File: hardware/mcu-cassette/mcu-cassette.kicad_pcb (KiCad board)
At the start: 2 copper layers, 80.4 x 50 mm, 4 parts, among them J1 02x15_Horinzontal_Header

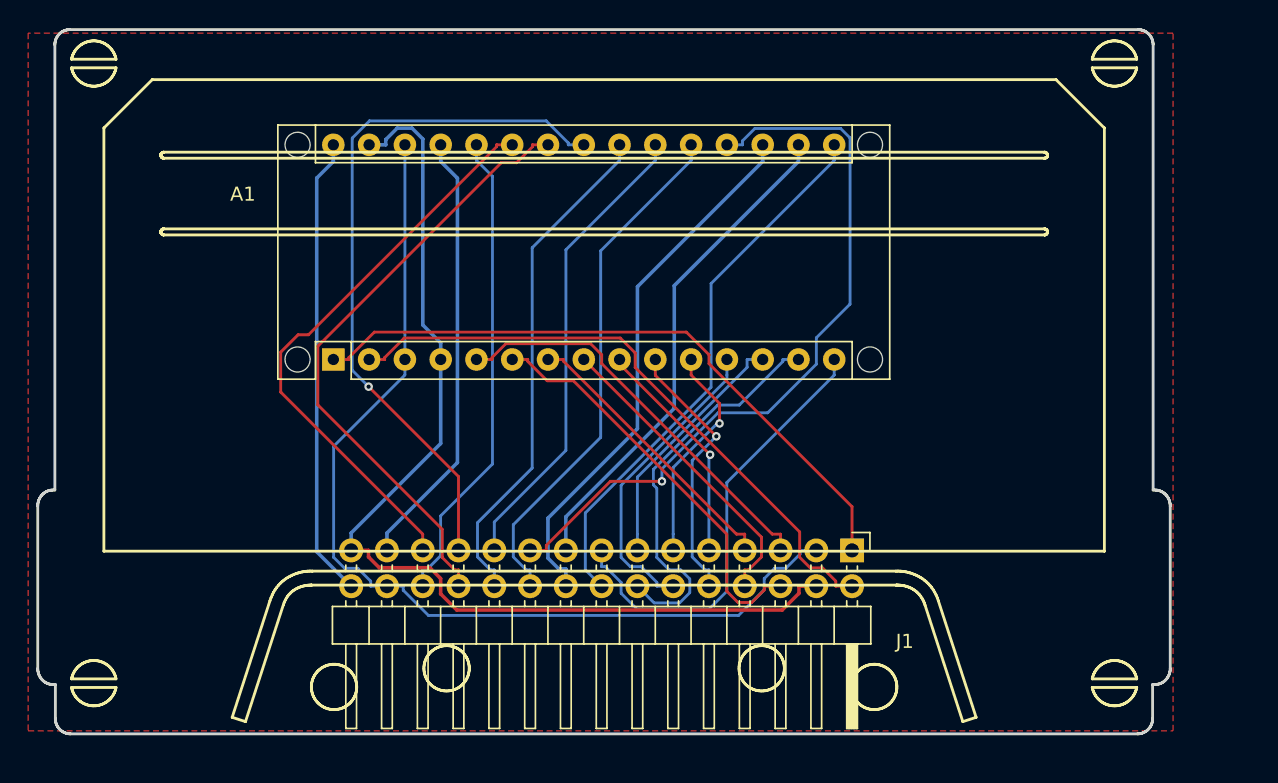
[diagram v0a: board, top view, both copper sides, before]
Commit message: [hw] Move copper pour to back layer, Add signature, Update pcb images
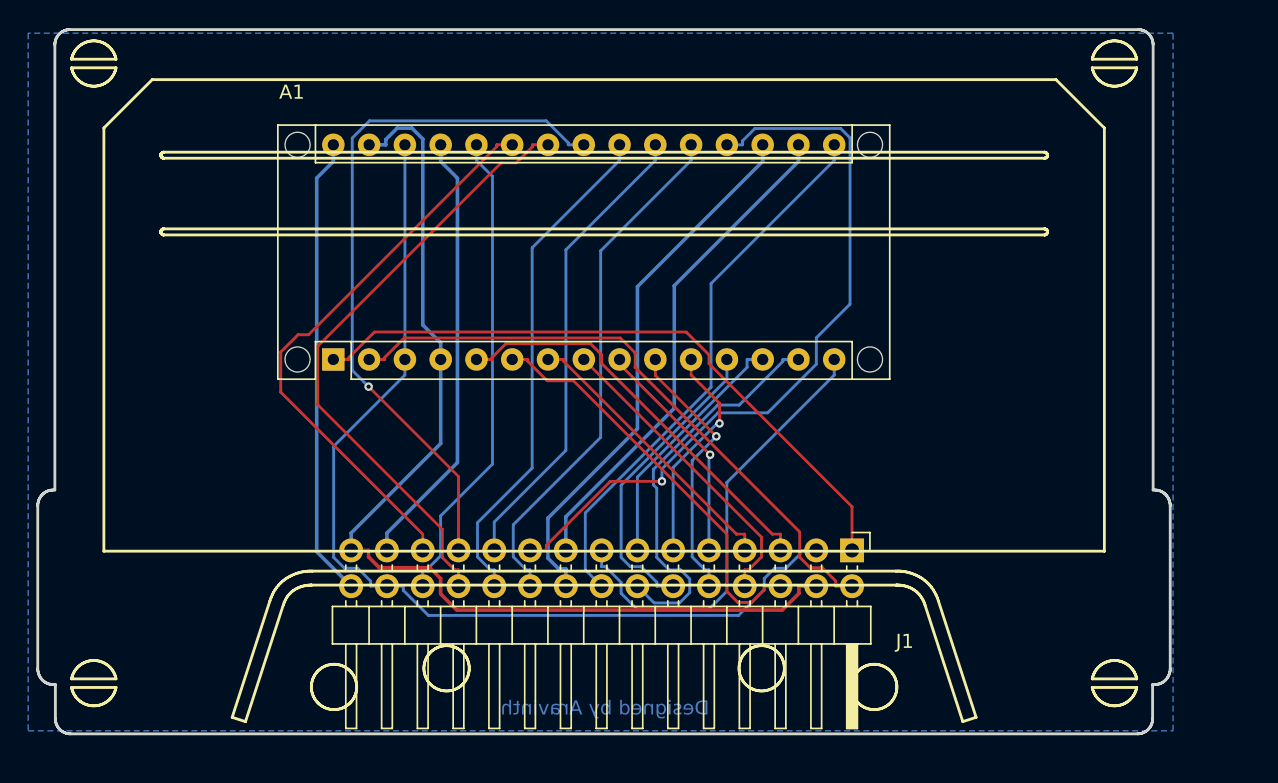
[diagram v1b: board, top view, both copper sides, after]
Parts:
- added REF**: CASSETTE-MARK, ARABEAT:CASSETTE-MARK, F.Cu at (94.5, 98.6)
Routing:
- added copper zone on B.Cu, net GND
- removed copper zone on F.Cu, net GND
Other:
- board text added: "Designed by Aravinth"

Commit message: [hw] Update libraries of MCU Cassette
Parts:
- G***: footprint ARABEAT:LOGO -> MCU-CASSETTE:LOGO
- REF**: footprint ARABEAT:CASSETTE-MARK -> MCU-CASSETTE:CASSETTE-MARK
- REF**: footprint ARABEAT:CASSETTE-SILKSCREEN -> MCU-CASSETTE:CASSETTE-SILKSCREEN

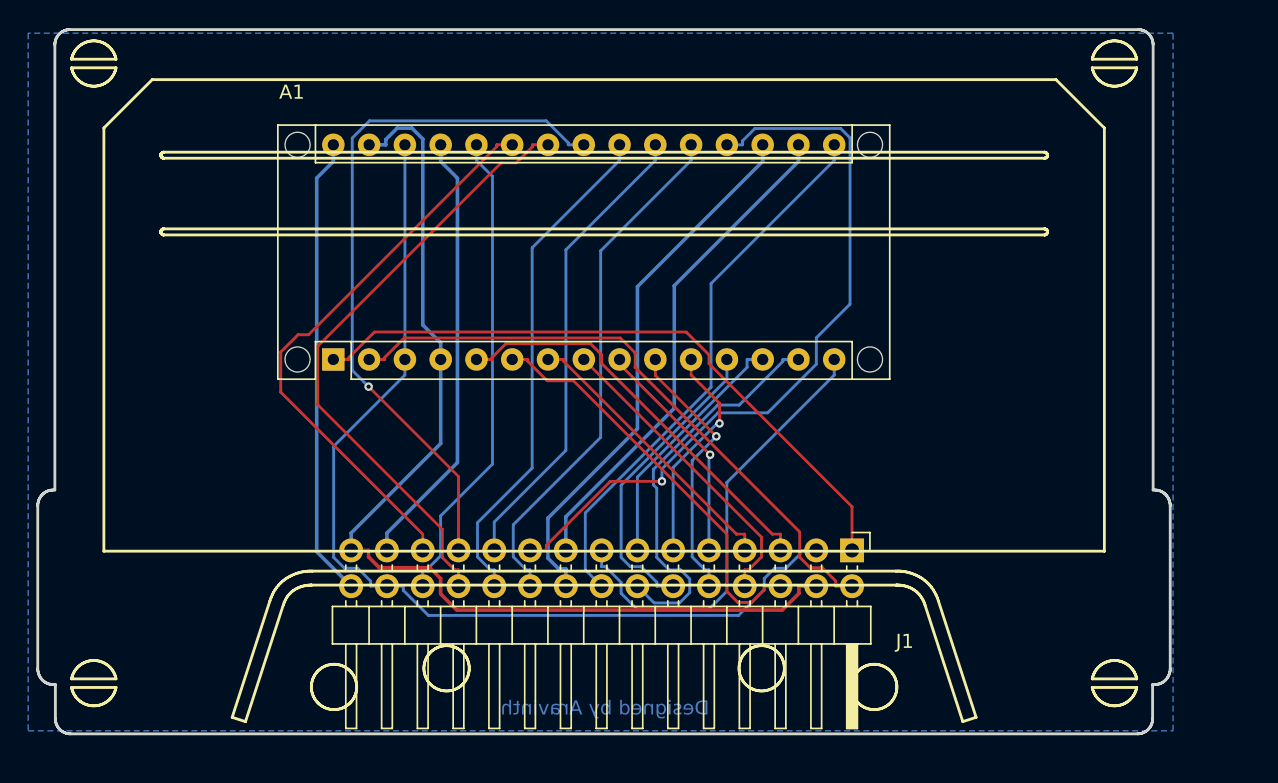
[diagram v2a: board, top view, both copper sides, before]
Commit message: [hw] Update MCU Cassette with new footprints
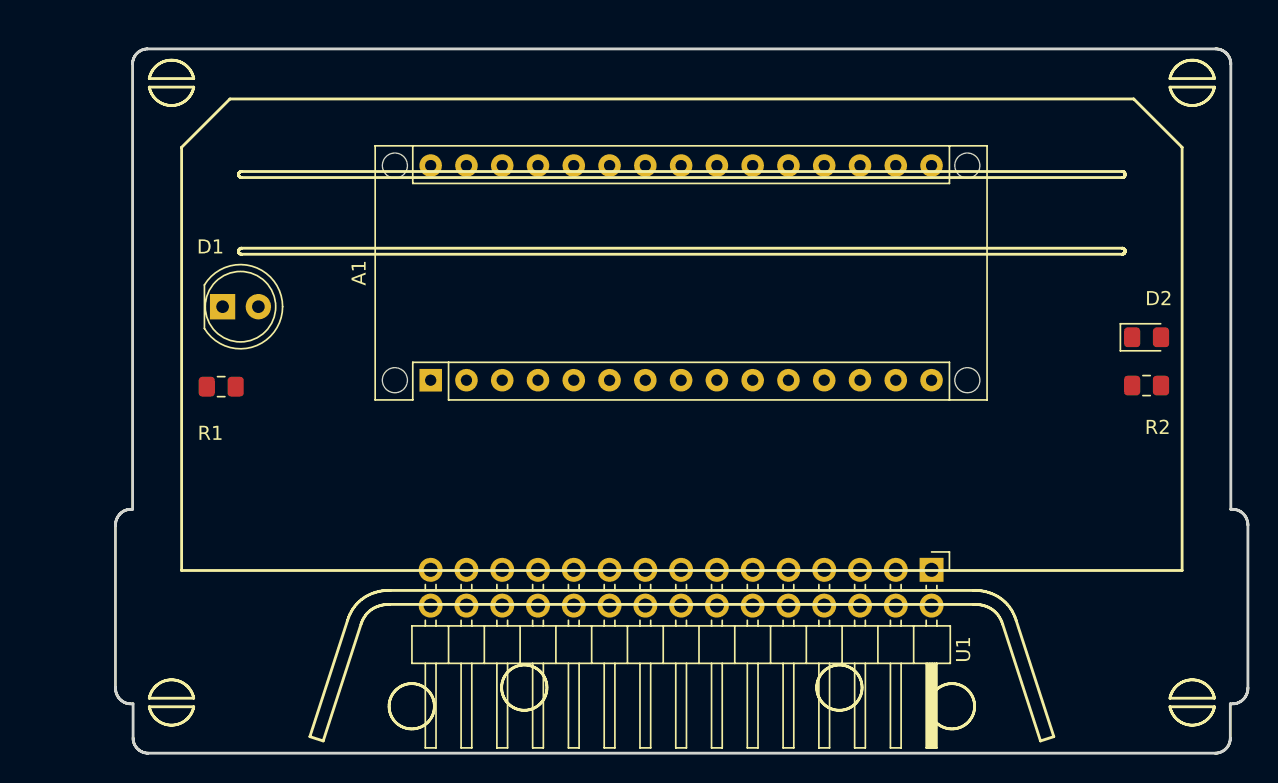
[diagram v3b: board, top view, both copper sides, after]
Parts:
- removed the G*** at (133.3, 119.4)
- removed J1: 02x15_Horinzontal_Header, Connector_PinHeader_2.54mm:PinHeader_2x15_P2.54mm_Horizontal
- removed the REF** at (94.5, 98.6) (x2)
- added D1: RED_HEART_LED, LED_THT:LED_D5.0mm, F.Cu at (107.8, 118.5)
- added D2: GREEN_PWR_LED, LED_SMD:LED_0805_2012Metric_Pad1.15x1.40mm_HandSolder, F.Cu at (173.4, 120.7)
- added G***: LOGO, ARABEAT:MCU-CASSETTE-LOGO, B.Cu at (140.4, 121.0)
- added R1: 1K, Resistor_SMD:R_0805_2012Metric_Pad1.15x1.40mm_HandSolder, F.Cu at (107.7, 124.2)
- added R2: 1K, Resistor_SMD:R_0805_2012Metric_Pad1.15x1.40mm_HandSolder, F.Cu at (173.4, 124.1)
- added REF**: CASSETTE-SILKSCREEN, ARABEAT:MCU-CASSETTE-SILKSCREEN-EDGECUT, F.Cu at (100.0, 100.0)
- added REF**: CASSETTE-MARK, ARABEAT:MCU-CASSETTE-MARK, F.Cu at (100.0, 100.0)
- added U1: 02x15_PIN_HEADER_SOCKET, Connector_PinHeader_2.54mm:PinHeader_2x15_P2.54mm_Horizontal, F.Cu at (158.1, 137.2)
- moved A1 7.06 mm to (122.6, 123.7)
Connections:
- A1 pad 17: 3V3 -> (no net)
- A1 pad 30: VIN -> (no net)
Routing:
- net GND: track 73.9 -> 0.00 mm
- net RST: track 70.3 -> 0.00 mm
- net A0: track 53.2 -> 0.00 mm, vias 1 -> 0
- net A4: track 50.1 -> 0.00 mm, vias 1 -> 0
- net D1: track 46.3 -> 0.00 mm
- net D0: track 44.2 -> 0.00 mm
- net A5: track 43.7 -> 0.00 mm
- net A6: track 40.9 -> 0.00 mm
- net D13: track 39.1 -> 0.00 mm
- net AREF: track 38.5 -> 0.00 mm
- net A1: track 37.2 -> 0.00 mm
- net A3: track 36.2 -> 0.00 mm
- net 3V3: track 35.6 -> 0.00 mm
- net A7: track 34.0 -> 0.00 mm
- net A2: track 33.5 -> 0.00 mm
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- removed copper zone on B.Cu, net GND
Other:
- net class PWR removed
- net class SIGNAL removed
- rule trace_min: 0.1524 -> 0.2
- rule via_min_size: 0.6 -> 0.4
- board text removed: "Designed by Aravinth"

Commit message: [hw] Update MCU cassette schematics, layout, footprints
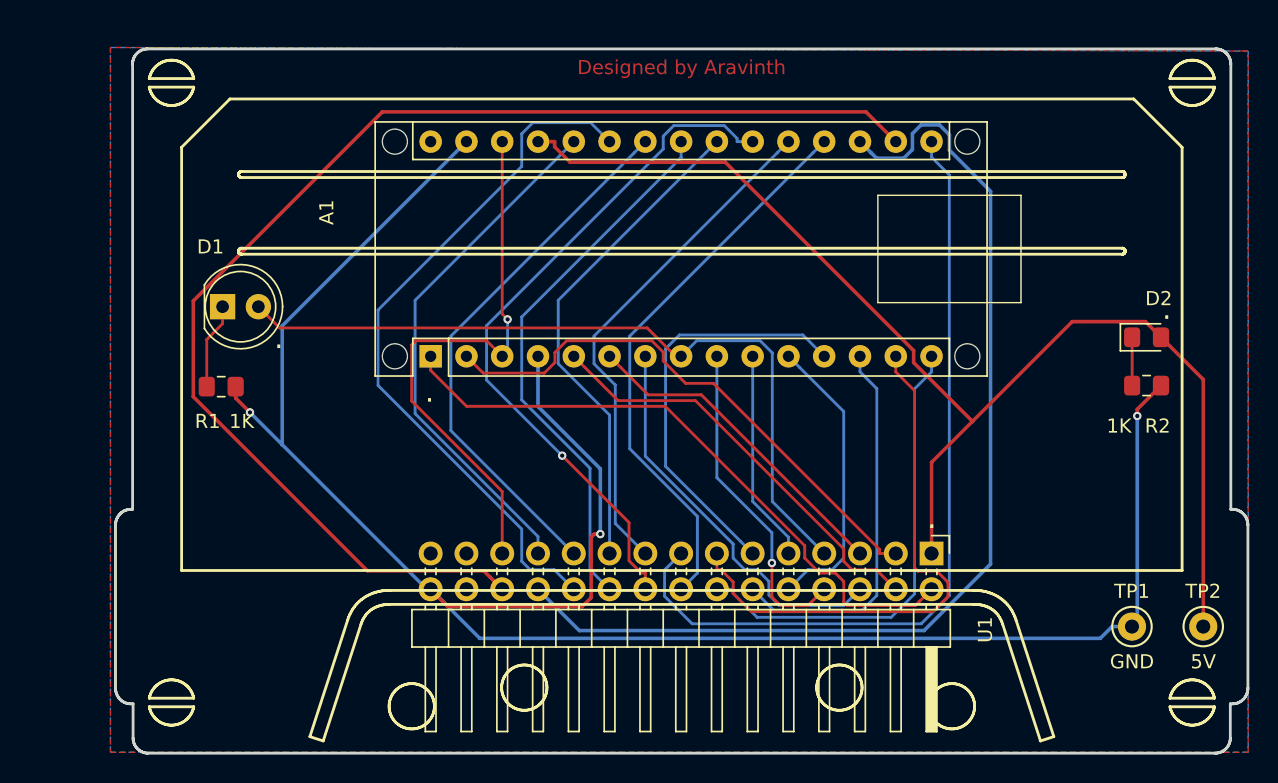
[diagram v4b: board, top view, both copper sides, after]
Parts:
- removed the G*** at (140.4, 121.0)
- added G***: LOGO, ARABEAT:CASSETTE-LOGO, B.Cu at (140.3, 129.3)
- added TP1: GND, TestPoint:TestPoint_Keystone_5000-5004_Miniature, F.Cu at (172.3, 141.2)
- added TP2: 5V, TestPoint:TestPoint_Keystone_5000-5004_Miniature, F.Cu at (177.4, 141.2)
- A1: footprint Module:Arduino_Nano_WithMountingHoles -> ARABEAT:Arduino_Nano_WithMountingHoles
- moved A1 1.70 mm to (122.6, 122.0)
- moved U1 1.16 mm to (158.1, 136.0)
- renumbered REF** to SLK-FR, REF** to SLK-MK
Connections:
- A1 pad 17: (no net) -> 3V3
- U1 pad 26: (no net) -> 3V3
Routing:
- net GND: track 0.00 -> 149.4 mm, vias 0 -> 3
- net 3V3: track 0.00 -> 90.7 mm
- net 5V: track 0.00 -> 88.9 mm
- net AREF: track 0.00 -> 75.8 mm
- net D13: track 0.00 -> 58.1 mm
- net D5: track 0.00 -> 54.5 mm
- net A6: track 0.00 -> 50.4 mm
- net A2: track 0.00 -> 49.5 mm, vias 0 -> 1
- net D1: track 0.00 -> 45.3 mm
- net RST: track 0.00 -> 40.0 mm, vias 0 -> 1
- net A0: track 0.00 -> 40.0 mm
- net D0: track 0.00 -> 39.1 mm
- net D11: track 0.00 -> 39.1 mm
- net A4: track 0.00 -> 39.0 mm
- net A5: track 0.00 -> 38.6 mm
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- added copper zone on F.Cu, net 5V
- added copper zone on B.Cu, net GND
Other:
- net class PWR added: clearance 0.254, trace_width 0.254, via_dia 0.6, via_drill 0.3
- net class SIGNAL added: clearance 0.2032, trace_width 0.2032, via_dia 0.6, via_drill 0.3
- rule trace_min: 0.2 -> 0.1524
- rule via_min_size: 0.4 -> 0.6
- board text added: "."
- board text added: "Designed by Aravinth"
- board text added: "ECG Module v0.2 : Designed by Aravinth"
- board text added: "www.arabeat.aravinth.info"
